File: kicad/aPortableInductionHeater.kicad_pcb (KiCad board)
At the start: 2 copper layers, 160.3 x 50.8 mm, 27 parts, among them U1 schUCC27211, U2 schUCC27211, U3 schTLV1117-33

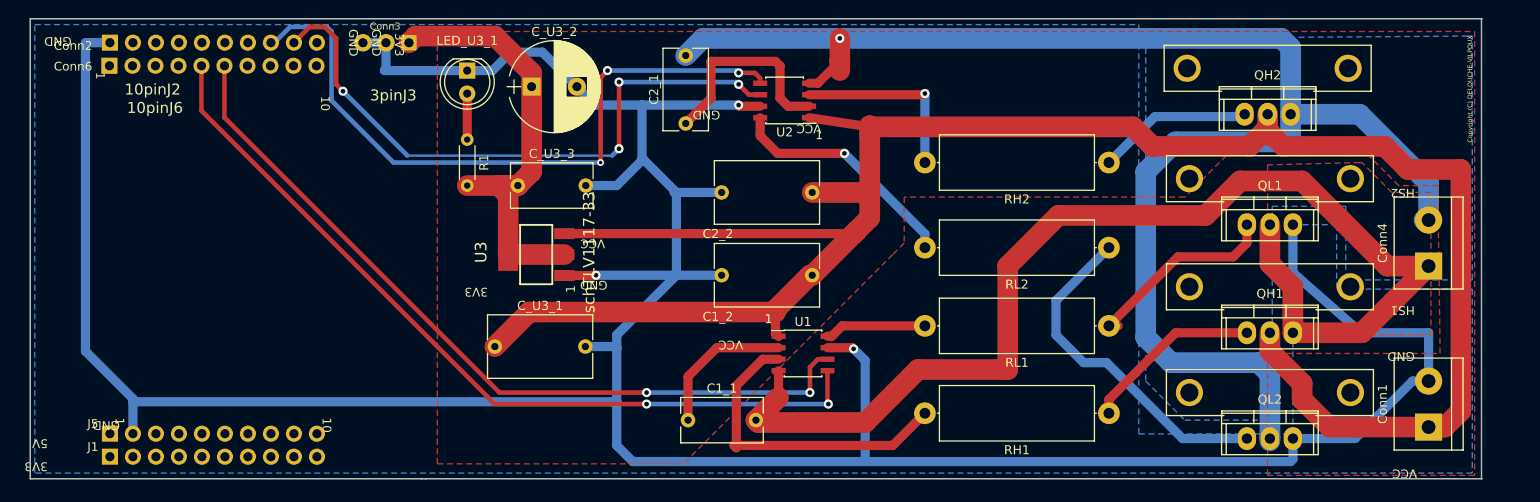
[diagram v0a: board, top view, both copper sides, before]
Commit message: changed fp IRFB4110
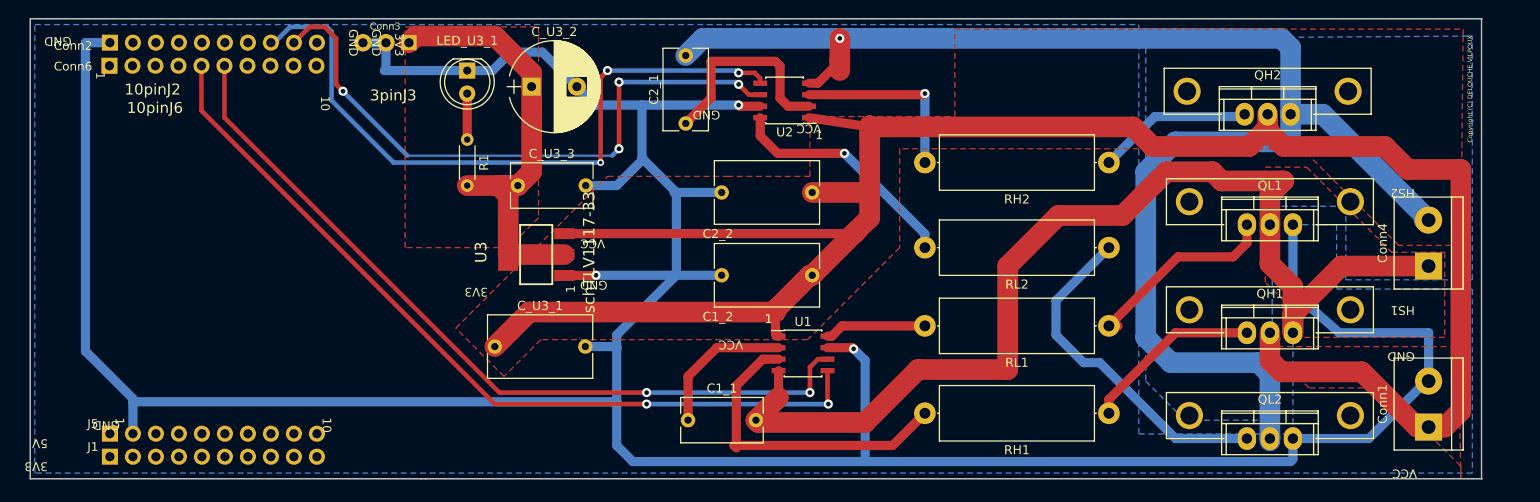
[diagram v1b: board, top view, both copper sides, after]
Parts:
- QH1, QH2, QL1, QL2: footprint UCC27211:TO-220-HeatSinkHoles -> ucc27211:TO-220-HeatSinkHoles
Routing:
- net HS1: track 133.6 -> 121.1 mm
- net HS2: track 168.0 -> 165.6 mm
- net GND: track 368.3 -> 369.7 mm
- added copper zone on F.Cu, net 3V3

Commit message: Name&Version of the product
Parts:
- moved C1_2 4.35 mm to (172.5, 122.9)
- moved C_U3_2 4.35 mm to (141.5, 102.1)
- moved J1 4.35 mm to (106.3, 143.0)
- moved J5 4.35 mm to (106.3, 140.4)
- moved QH1 4.35 mm to (223.0, 129.3)
- moved QH2 4.35 mm to (222.8, 105.2)
- moved QL2 4.35 mm to (223.0, 141.0)
- moved R1 4.35 mm to (134.4, 108.0)
- moved RL1 4.35 mm to (205.2, 128.5)
- moved RL2 4.35 mm to (205.2, 119.9)
- moved U2 4.35 mm to (169.4, 103.6)
- moved C2_1 4.35 mm to (158.5, 106.2)
- moved C2_2 4.35 mm to (172.5, 113.8)
- moved C_U3_3 4.35 mm to (140.0, 113.0)
- moved Conn4 4.35 mm to (240.5, 121.9)
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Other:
- board text added: "aPortableInductionHeater - V1.0"
